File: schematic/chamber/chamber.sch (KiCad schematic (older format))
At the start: 10 parts

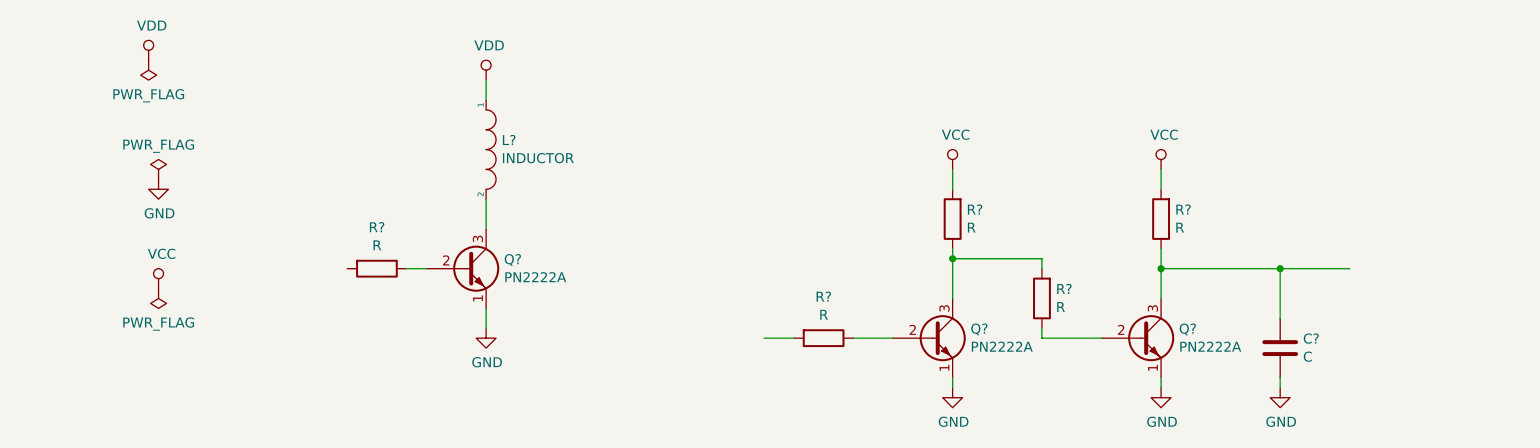
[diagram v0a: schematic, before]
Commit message: label ins and outs on schematic
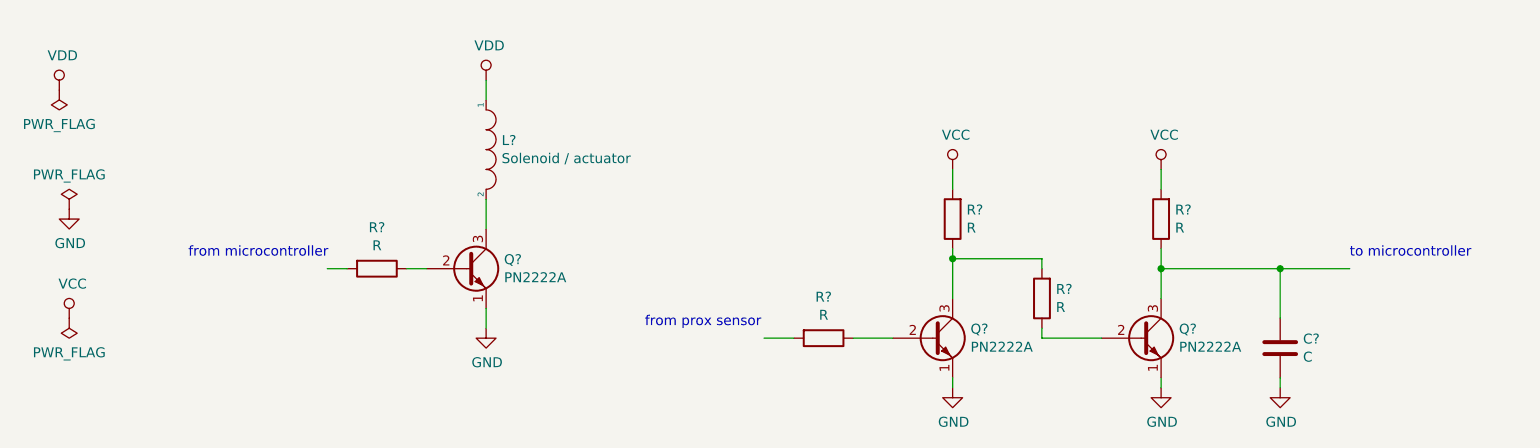
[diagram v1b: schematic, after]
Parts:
- L?: value INDUCTOR -> Solenoid / actuator
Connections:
- wire segments 22 -> 23
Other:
- note added: "from microcontroller"
- note added: "from prox sensor"
- note added: "to microcontroller"
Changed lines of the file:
@@
 L power:VCC #PWR?
 U 1 1 5DD5080B
-P 1650 3200
-F 0 "#PWR?" H 1650 3050 50  0001 C CNN
-F 1 "VCC" H 1667 3373 50  0000 C CNN
-F 2 "" H 1650 3200 50  0001 C CNN
-F 3 "" H 1650 3200 50  0001 C CNN
-	1    1650 3200
+P 1200 3350
+F 0 "#PWR?" H 1200 3200 50  0001 C CNN
+F 1 "VCC" H 1217 3523 50  0000 C CNN
+F 2 "" H 1200 3350 50  0001 C CNN
+F 3 "" H 1200 3350 50  0001 C CNN
+	1    1200 3350
 	1    0    0    -1
 $EndComp
@@
 L power:PWR_FLAG #FLG?
 U 1 1 5DD511A1
-P 1650 3200
-F 0 "#FLG?" H 1650 3275 50  0001 C CNN
-F 1 "PWR_FLAG" H 1650 3373 50  0000 C CNN
-F 2 "" H 1650 3200 50  0001 C CNN
-F 3 "~" H 1650 3200 50  0001 C CNN
-	1    1650 3200
+P 1200 3350
+F 0 "#FLG?" H 1200 3425 50  0001 C CNN
+F 1 "PWR_FLAG" H 1200 3523 50  0000 C CNN
+F 2 "" H 1200 3350 50  0001 C CNN
+F 3 "~" H 1200 3350 50  0001 C CNN
+	1    1200 3350
 	-1   0    0    1
 $EndComp
@@
 L power:GND #PWR?
 U 1 1 5DD52510
-P 1650 2650
-F 0 "#PWR?" H 1650 2400 50  0001 C CNN
-F 1 "GND" H 1655 2477 50  0000 C CNN
-F 2 "" H 1650 2650 50  0001 C CNN
-F 3 "" H 1650 2650 50  0001 C CNN
-	1    1650 2650
+P 1200 2800
+F 0 "#PWR?" H 1200 2550 50  0001 C CNN
+F 1 "GND" H 1205 2627 50  0000 C CNN
+F 2 "" H 1200 2800 50  0001 C CNN
+F 3 "" H 1200 2800 50  0001 C CNN
+	1    1200 2800
 	1    0    0    -1
 $EndComp
@@
 L power:PWR_FLAG #FLG?
 U 1 1 5DD5393E
-P 1650 2650
-F 0 "#FLG?" H 1650 2725 50  0001 C CNN
-F 1 "PWR_FLAG" H 1650 2823 50  0000 C CNN
-F 2 "" H 1650 2650 50  0001 C CNN
-F 3 "~" H 1650 2650 50  0001 C CNN
-	1    1650 2650
+P 1200 2800
+F 0 "#FLG?" H 1200 2875 50  0001 C CNN
+F 1 "PWR_FLAG" H 1200 2973 50  0000 C CNN
+F 2 "" H 1200 2800 50  0001 C CNN
+F 3 "~" H 1200 2800 50  0001 C CNN
+	1    1200 2800
 	1    0    0    -1
 $EndComp
@@
 P 3300 2500
 F 0 "L?" V 3254 2578 50  0000 L CNN
-F 1 "INDUCTOR" V 3345 2578 50  0000 L CNN
+F 1 "Solenoid / actuator" V 3345 2578 50  0000 L CNN
 F 2 "" H 3300 2500 50  0001 C CNN
 F 3 "~" H 3300 2500 50  0001 C CNN
@@
 L power:PWR_FLAG #FLG?
 U 1 1 5DD6685A
-P 1600 2050
-F 0 "#FLG?" H 1600 2125 50  0001 C CNN
-F 1 "PWR_FLAG" H 1600 2223 50  0000 C CNN
-F 2 "" H 1600 2050 50  0001 C CNN
-F 3 "~" H 1600 2050 50  0001 C CNN
-	1    1600 2050
+P 1150 2200
+F 0 "#FLG?" H 1150 2275 50  0001 C CNN
+F 1 "PWR_FLAG" H 1150 2373 50  0000 C CNN
+F 2 "" H 1150 2200 50  0001 C CNN
+F 3 "~" H 1150 2200 50  0001 C CNN
+	1    1150 2200
 	-1   0    0    1
 $EndComp
@@
 L power:VDD #PWR?
 U 1 1 5DD677AE
-P 1600 2050
-F 0 "#PWR?" H 1600 1900 50  0001 C CNN
-F 1 "VDD" H 1617 2223 50  0000 C CNN
-F 2 "" H 1600 2050 50  0001 C CNN
-F 3 "" H 1600 2050 50  0001 C CNN
-	1    1600 2050
+P 1150 2200
+F 0 "#PWR?" H 1150 2050 50  0001 C CNN
+F 1 "VDD" H 1167 2373 50  0000 C CNN
+F 2 "" H 1150 2200 50  0001 C CNN
+F 3 "" H 1150 2200 50  0001 C CNN
+	1    1150 2200
 	1    0    0    -1
 $EndComp
@@
 Wire Wire Line
 	4850 3450 4700 3450
+Text Notes 4100 3400 0    50   ~ 0
+from prox sensor
+Text Notes 7650 3050 0    50   ~ 0
+to microcontroller
+Text Notes 1800 3050 0    50   ~ 0
+from microcontroller
+Wire Wire Line
+	2500 3100 2600 3100
 $EndSCHEMATC

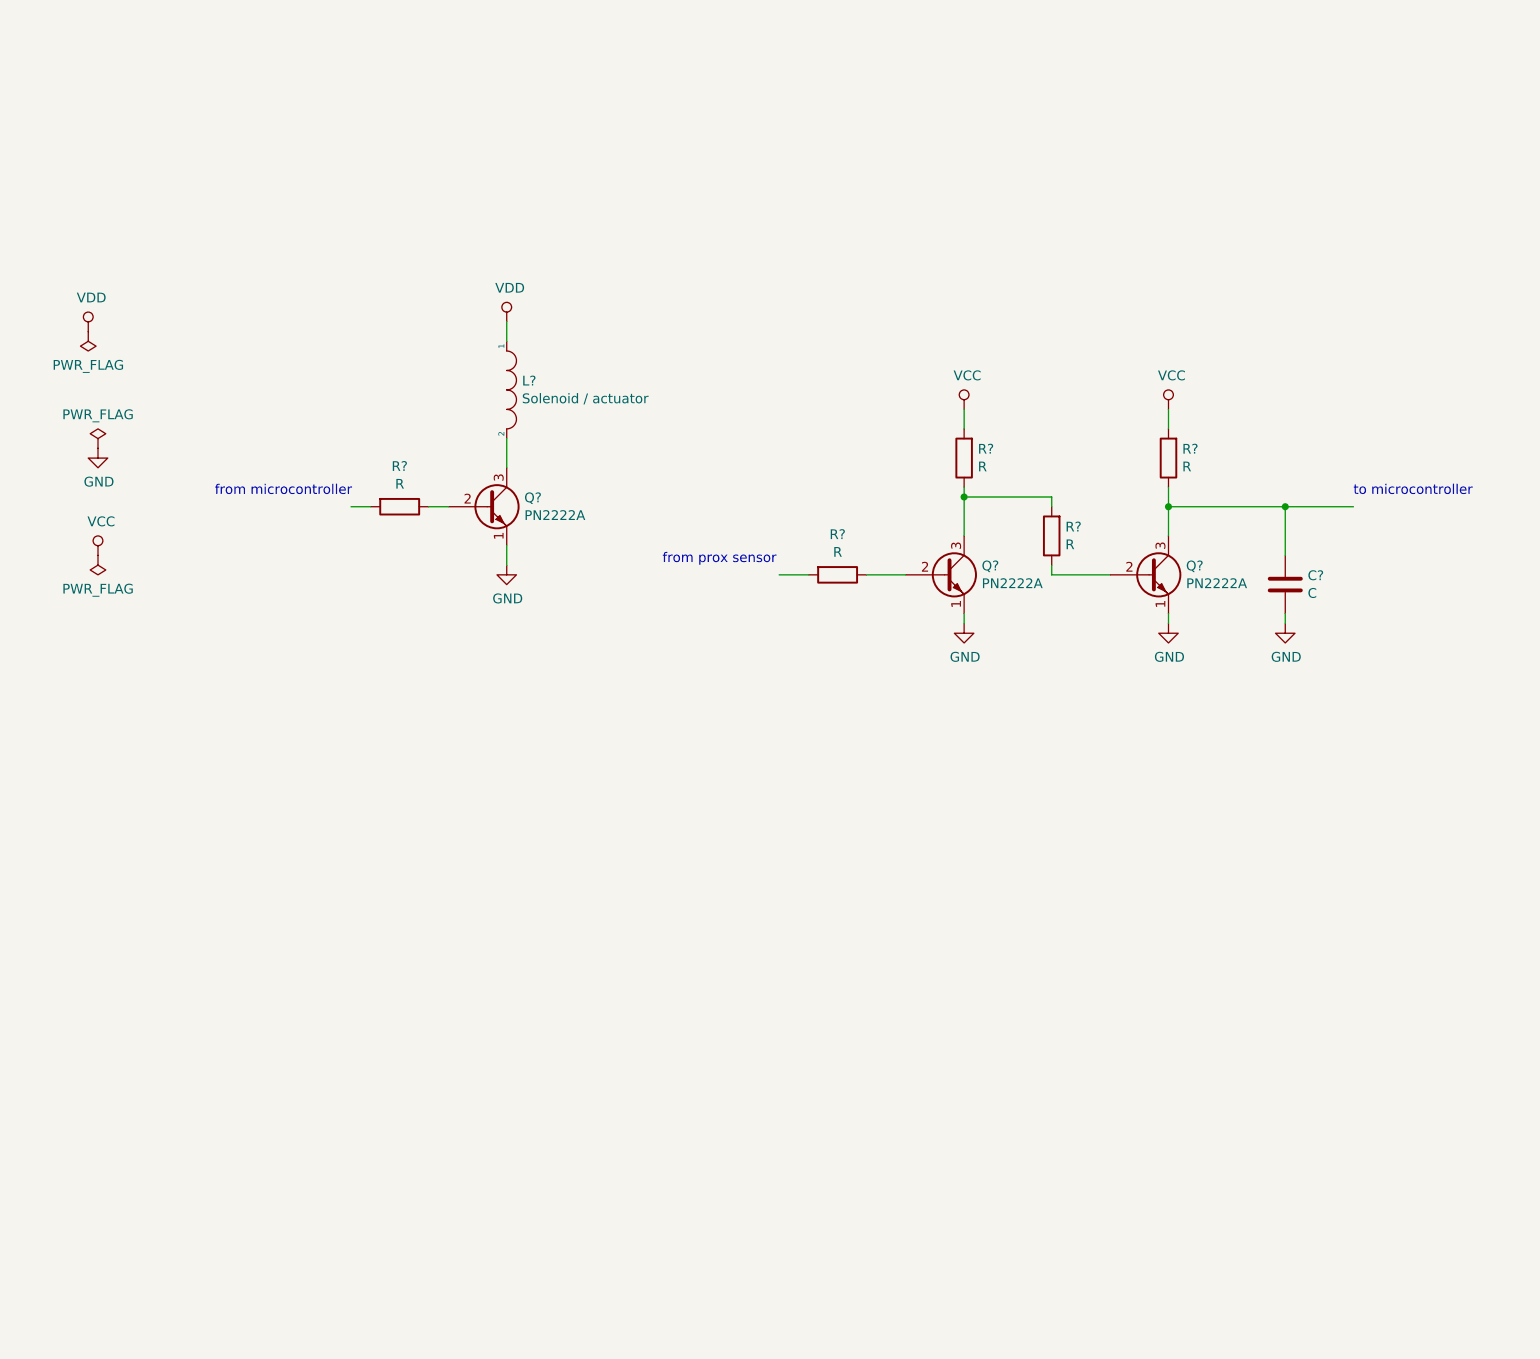
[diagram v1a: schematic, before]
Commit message: clean up repo add magazine schematic gnd both arduino in the schematic
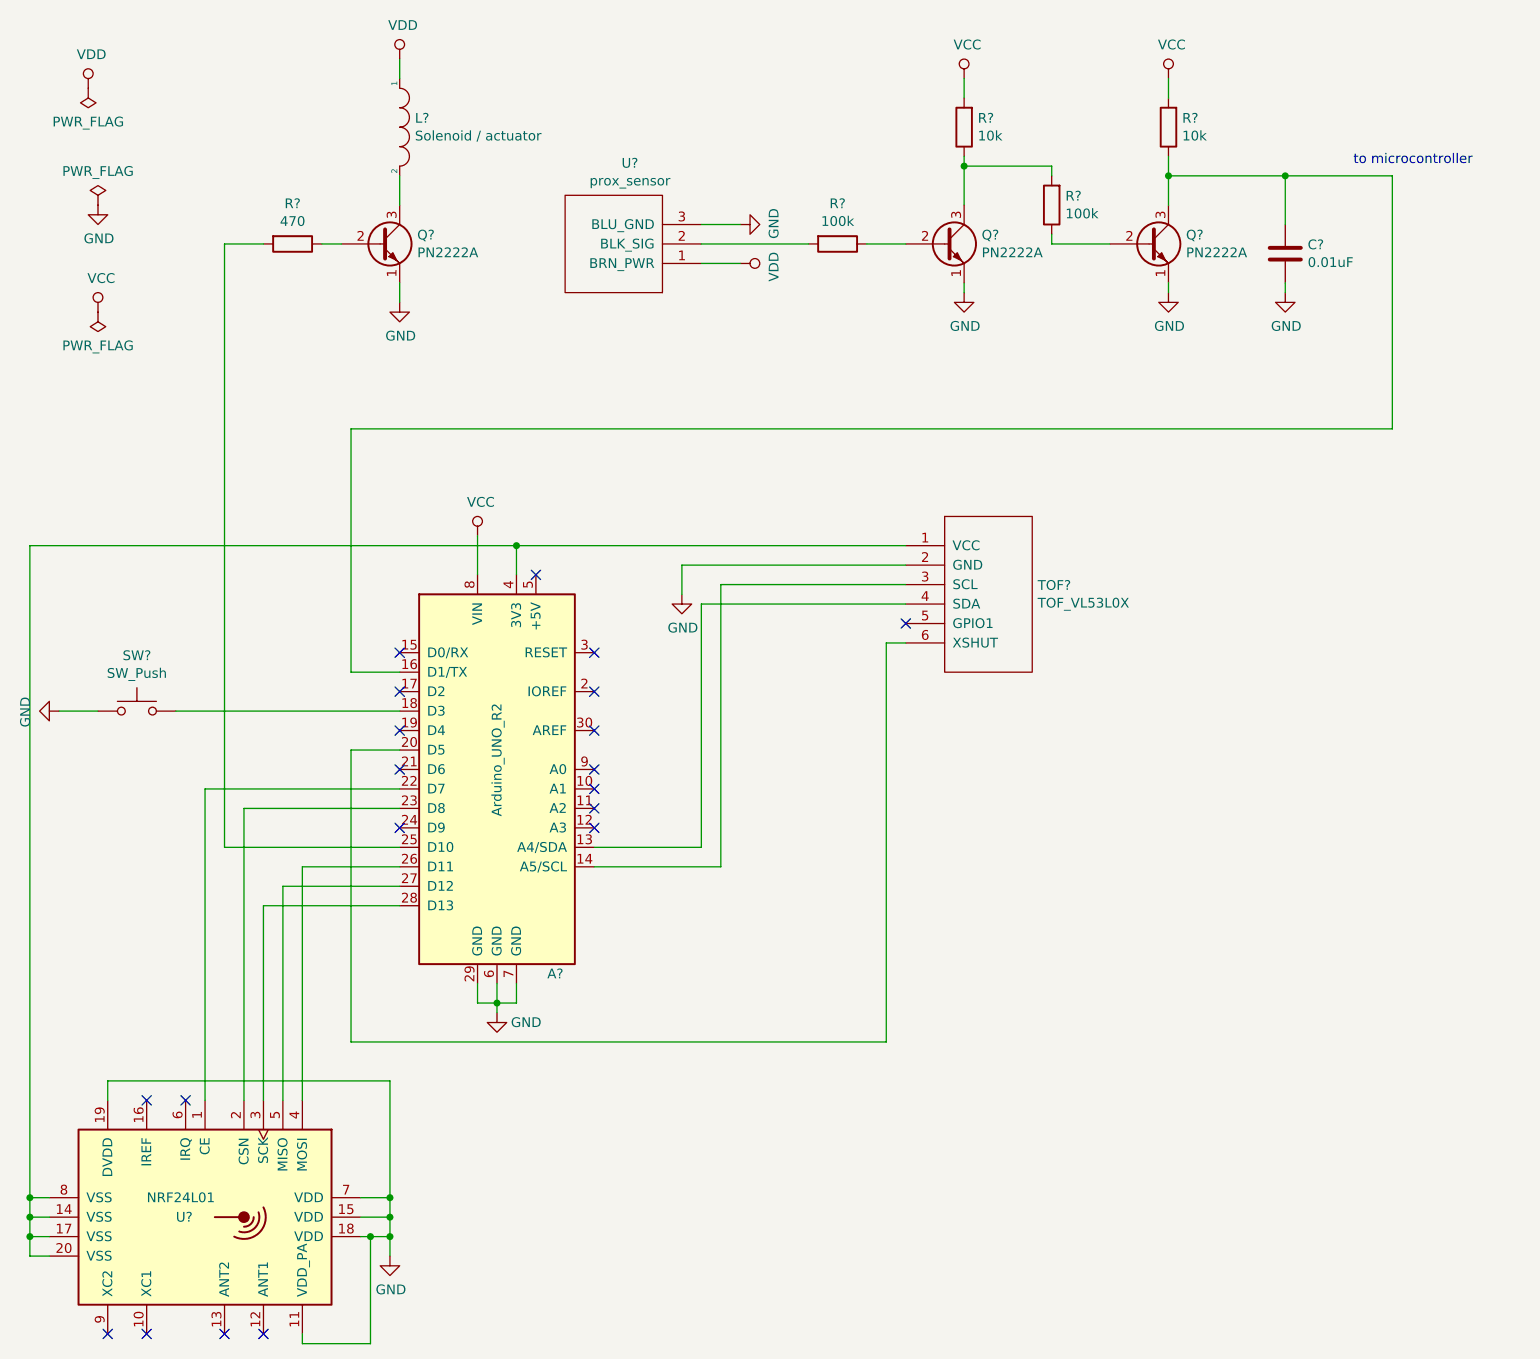
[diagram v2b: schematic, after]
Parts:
- added A?: Arduino_UNO_R2, Module:Arduino_UNO_R2, symbol MCU_Module:Arduino_UNO_R2
- added SW?: SW_Push, symbol Switch:SW_Push
- added TOF?: TOF_VL53L0X, symbol custom:TOF_VL53L0X
- added U?: prox_sensor, symbol custom:prox_sensor
- added U?: NRF24L01, Package_DFN_QFN:QFN-20-1EP_4x4mm_P0.5mm_EP2.5x2.5mm, symbol RF:NRF24L01
- C?: value C -> 0.01uF
- R?: value R -> 470
- R? (x2): value R -> 100k
- R? (x2): value R -> 10k
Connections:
- wire segments 23 -> 87
- no-connect marks 0 -> 20
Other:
- note removed: "from microcontroller"
- note removed: "from prox sensor"
- moved on the sheet: C?, L?, Q?, R?
